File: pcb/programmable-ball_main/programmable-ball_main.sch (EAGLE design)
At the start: 21 parts, among them J1 12402012E212A, P1 S2B-ZR-SM4A-TF, Q1 DMG2305UX-13, SW1 CAS-120CAS-120B1, U1 MDBT50Q-1MV2, U2 AP2112K-3.3TRG1, U3 MCP73832T-2ACI/OT, Y1 FC-135_32.7680KA-A0

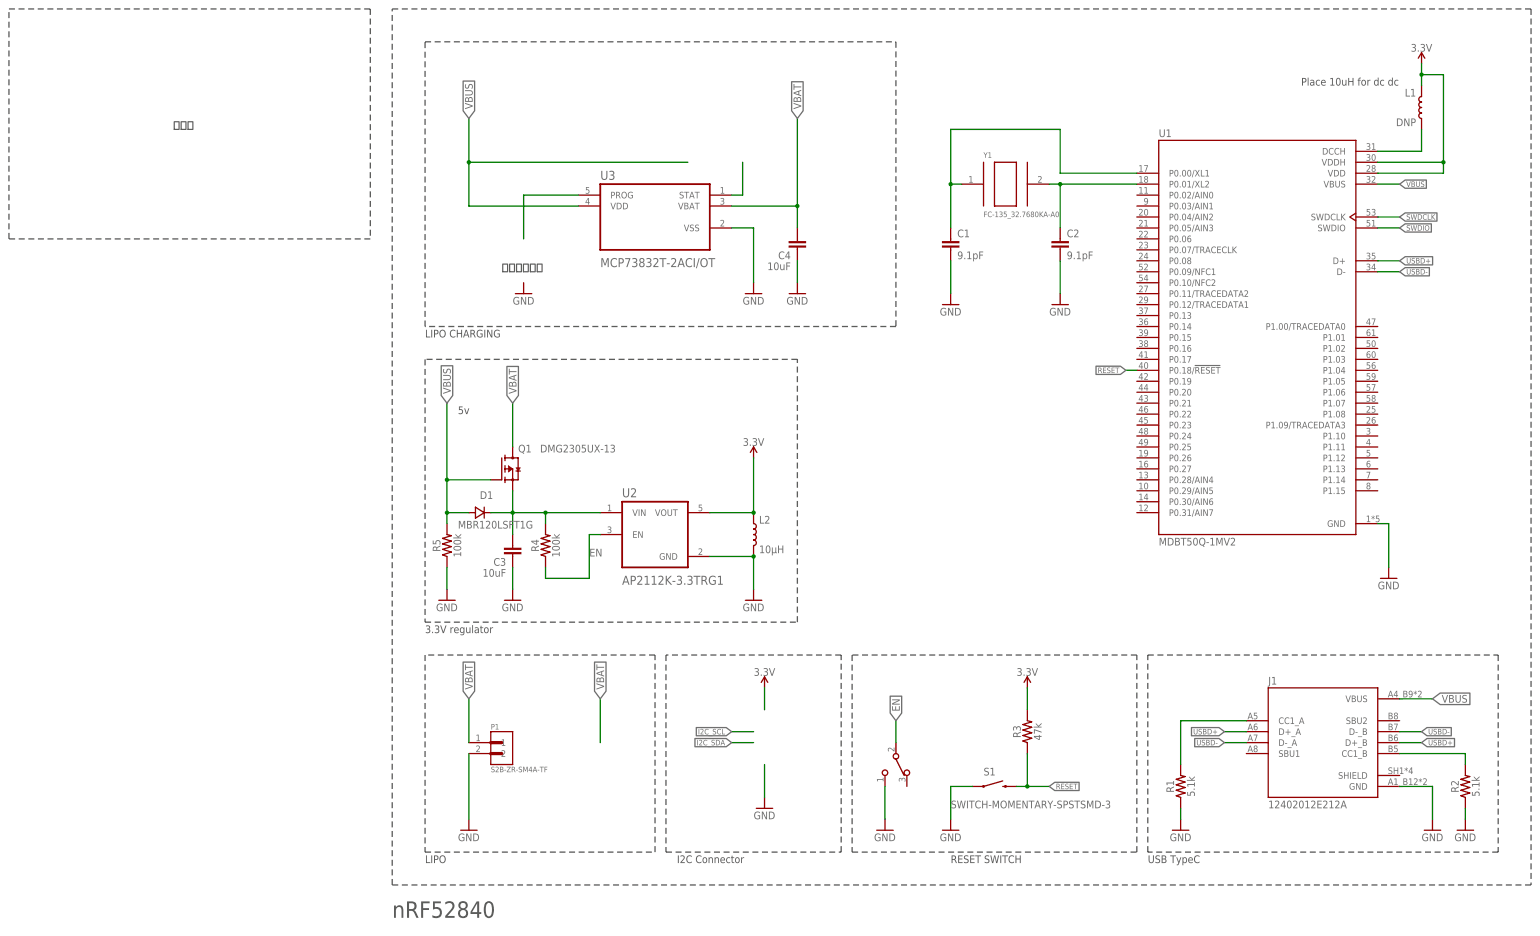
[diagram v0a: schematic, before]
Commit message: リポ充放電機能を搭載 #4
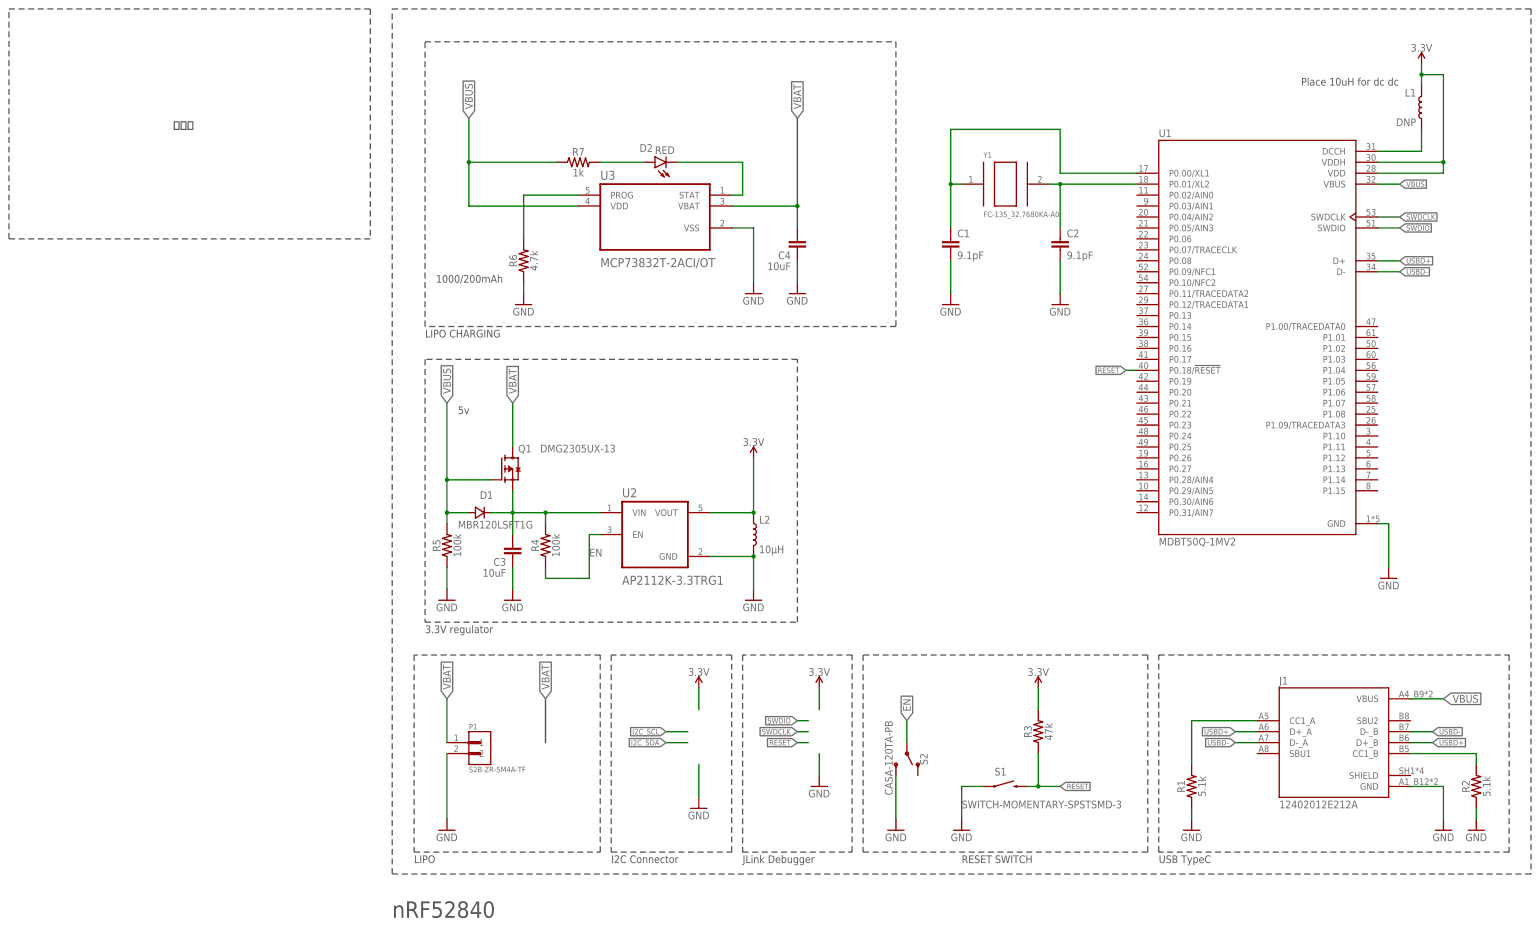
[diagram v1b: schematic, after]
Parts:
- removed SW1: CAS-120CAS-120B1, Switch:CAS-120CAS-120B1
- added D2: RED, SparkFun-LED:LED-RED_0402
- added R6: 4.7k, SparkFun-Resistors:4.7KOHM-0402T-1/16W-1%
- added R7: 1k, SparkFun-Resistors:1KOHM-0402T-1/16W-1%
- added S2: CASA-120TA-PB, CAS_120TA:CASA-120TA-PB
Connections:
- new net N$9: D2.A, R7.2
- net EN: now also S2.P; no longer SW1.2
- net GND: now also R6.1, S2.S; no longer SW1.1
- net N$7: now also R6.2
- net N$8: now also D2.C
- net VBUS: now also R7.1
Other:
- note added: "1000/200mAh"
- note added: "JLink Debugger"
- note removed: "抵抗値調べて"
- moved on the sheet: J1, P1, R1, R2, R3, S1

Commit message: パターンの位置調整
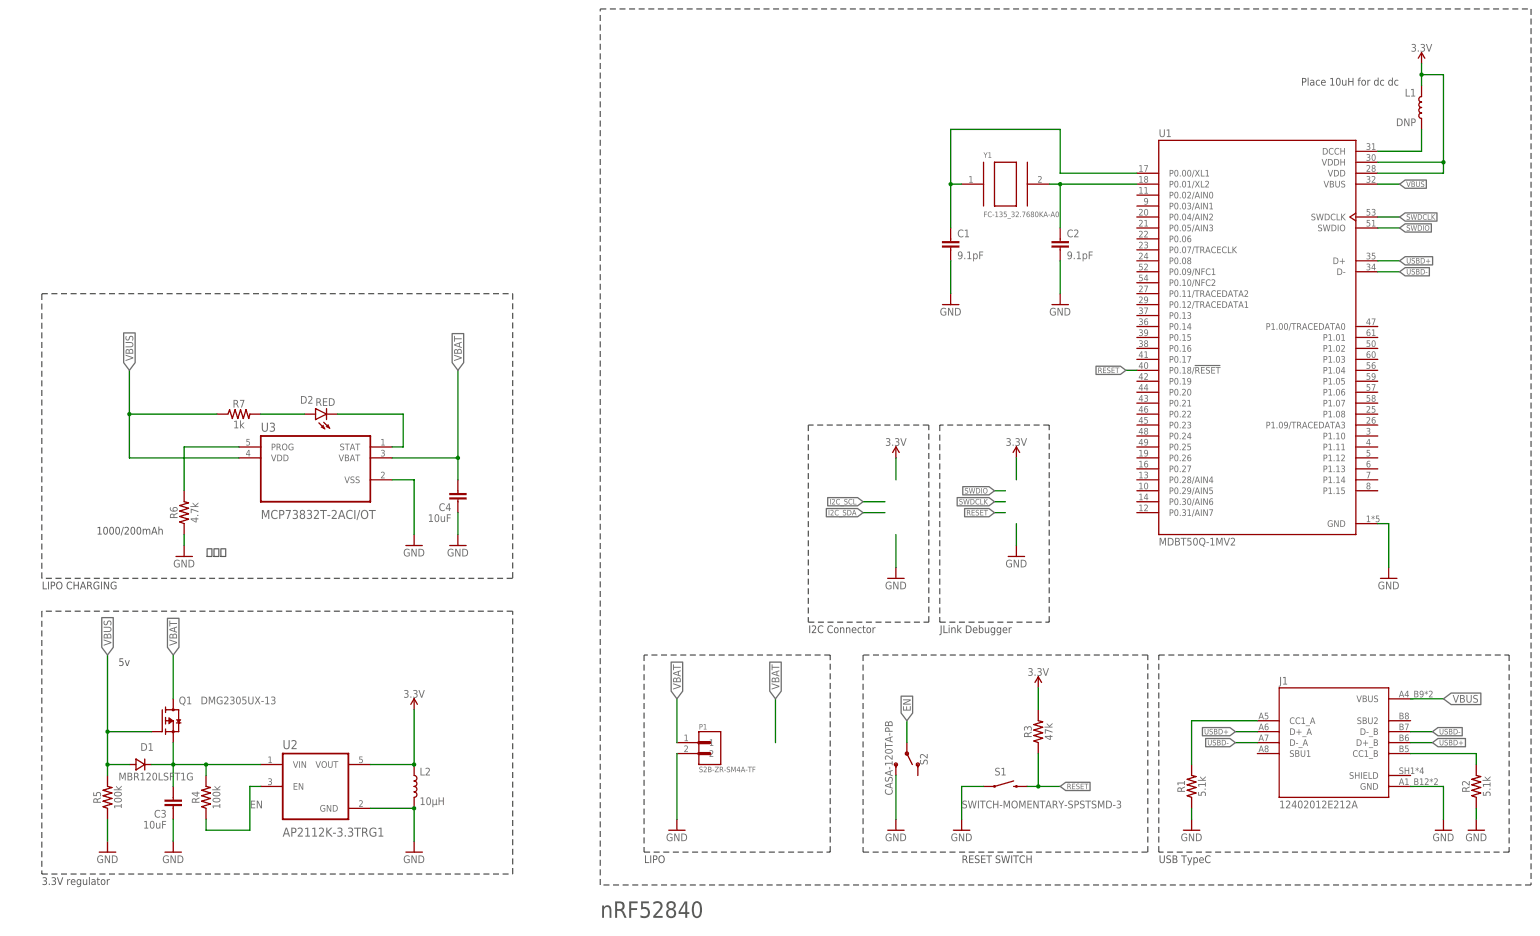
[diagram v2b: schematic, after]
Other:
- moved on the sheet: C3, C4, D1, D2, L2, P1, Q1, R4, R5, R6, R7, U2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

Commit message: コネクタとコンデンサを追加 #4
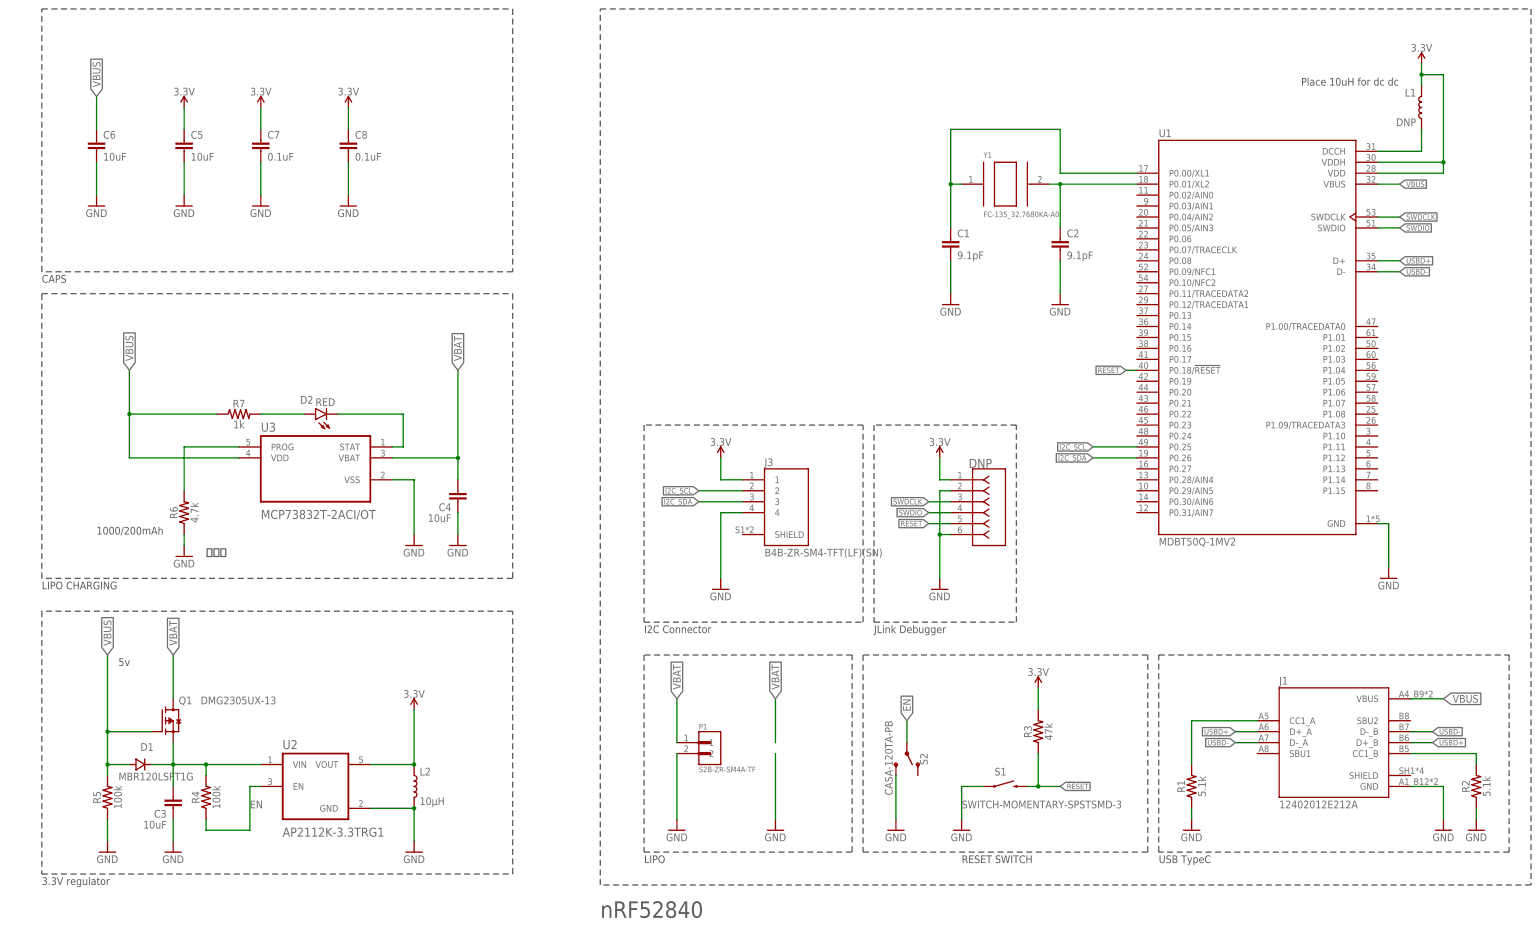
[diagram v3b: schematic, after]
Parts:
- added C5, C6: 10uF, SparkFun-Capacitors:10UF-0402T-6.3V-20%
- added C7, C8: 0.1uF, SparkFun-Capacitors:0.1UF-0402T-6.3V-10%-X7R
- added DNP: 84981-6RE, JtagConnector:84981-6RE
- added J3: B4B-ZR-SM4-TFT(LF)(SN), B4B-ZR-SM4-TFT_LF__SN_:B4B-ZR-SM4-TFT(LF)(SN)
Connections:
- new net I2C_SCL: J3.2, U1.P0.25
- new net I2C_SDA: J3.3, U1.P0.26
- net 3.3V: now also C5.1, C7.1, C8.1, DNP.1, J3.1
- net GND: now also C5.2, C6.2, C7.2, C8.2, DNP.2, DNP.6, J3.4
- net RESET: now also DNP.5
- net SWDCLK: now also DNP.3
- net SWDIO: now also DNP.4
- net VBUS: now also C6.1
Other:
- note added: "CAPS"

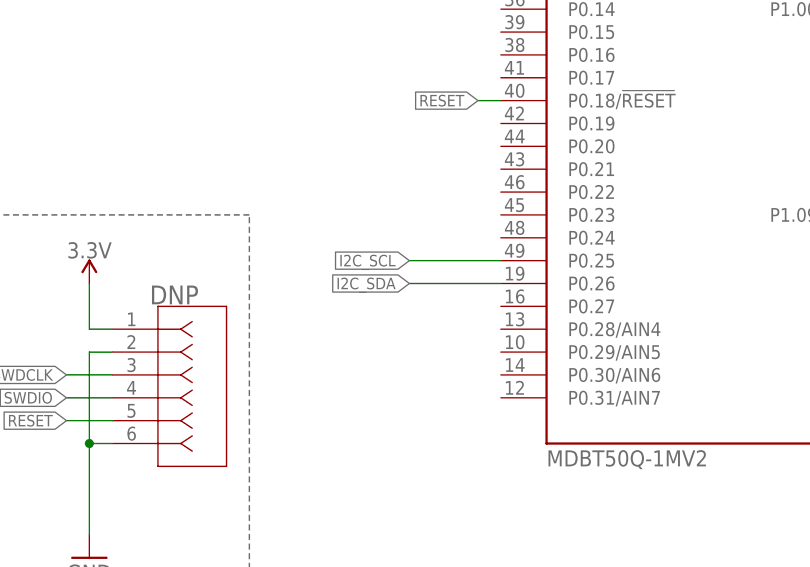
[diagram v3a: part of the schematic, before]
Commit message: 基板v1完成 resolved #4
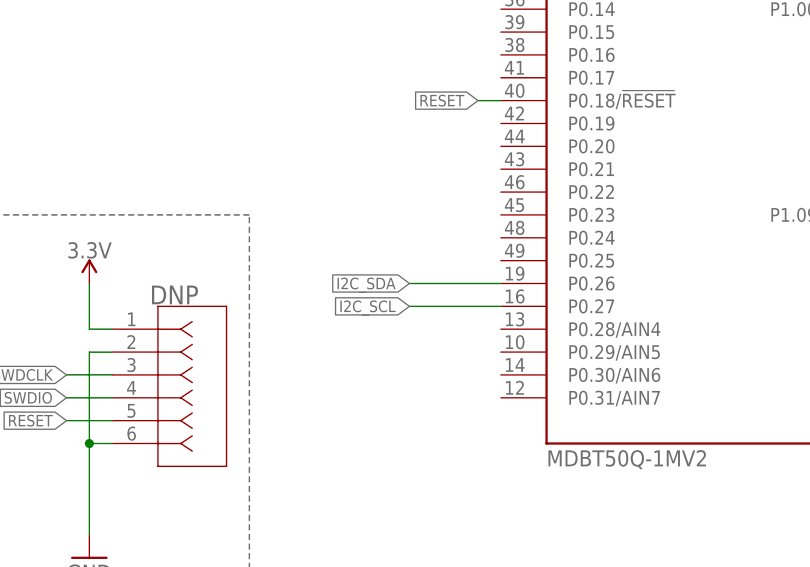
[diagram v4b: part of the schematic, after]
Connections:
- net I2C_SCL: now also U1.P0.27; no longer U1.P0.25
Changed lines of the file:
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@@
 </segment>
 <segment>
-<label x="266.7" y="139.7" size="1.27" layer="95" rot="R180" xref="yes"/>
-<wire x1="266.7" y1="139.7" x2="276.86" y2="139.7" width="0.1524" layer="91"/>
-<pinref part="U1" gate="G$1" pin="P0.25"/>
+<label x="266.7" y="134.62" size="1.27" layer="95" rot="R180" xref="yes"/>
+<pinref part="U1" gate="G$1" pin="P0.27"/>
+<wire x1="266.7" y1="134.62" x2="276.86" y2="134.62" width="0.1524" layer="91"/>
 </segment>
 </net>
@@
 </sheet>
 </sheets>
+<errors>
+</errors>
 </schematic>
 </drawing>

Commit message: v1の修正
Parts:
- added R10, R11: 100k, SparkFun-Resistors:100KOHM-0402T-1/16W-1%
- added R8, R9: 22Ω, SparkFun-Resistors:22OHM-0402T-1/16W-1%
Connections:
- new net N$10: R8.1, U1.D+
- new net N$11: R9.1, U1.D-
- new net VDIV: R10.1, R11.2, U1.P0.29/AIN5
- net GND: now also R11.1
- net USBD+: now also R8.2; no longer U1.D+
- net USBD-: now also R9.2; no longer U1.D-
- net VBAT: now also R10.2
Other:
- moved on the sheet: C7, C8, DNP, J3, P1, R3, S1, S2
